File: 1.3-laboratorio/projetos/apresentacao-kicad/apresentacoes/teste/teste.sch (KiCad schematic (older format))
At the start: 19 parts

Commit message: Em elaboração, questões para a P2/2020 de ETE103/N.
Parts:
- added U?: 74AHC04, symbol 74xx:74AHC04
- added U?: 74LS04, symbol 74xx:74LS04
- added U?: IR4302, Package_DFN_QFN:Infineon_PQFN-44-31-5EP_7x7mm_P0.5mm, symbol Amplifier_Audio:IR4302
- added U?: 4002, symbol 4xxx:4002
- added U?: LM339, symbol Comparator:LM339
- added U? (x2): 74LS00, symbol 74xx:74LS00
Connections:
- new net: U?.15 (COM), U?.28 (COM), U?.31 (COM)
- new net: U?.18 (VS1), U?.20 (VS1)
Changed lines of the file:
@@
+	1    0    0    -1
+$EndComp
+$Comp
+L 74xx:74AHC04 U?
+U 1 1 5FABFB5E
+P 5250 1450
+F 0 "U?" H 5250 1767 50  0000 C CNN
+F 1 "74AHC04" H 5250 1676 50  0000 C CNN
+F 2 "" H 5250 1450 50  0001 C CNN
+F 3 "https://assets.nexperia.com/documents/data-sheet/74AHC_AHCT04.pdf" H 5250 1450 50  0001 C CNN
+	1    5250 1450
+	1    0    0    -1
+$EndComp
+$Comp
+L 74xx:74LS04 U?
+U 2 1 5FAC08BE
+P 7000 1500
+F 0 "U?" H 7000 1817 50  0000 C CNN
+F 1 "74LS04" H 7000 1726 50  0000 C CNN
+F 2 "" H 7000 1500 50  0001 C CNN
+F 3 "http://www.ti.com/lit/gpn/sn74LS04" H 7000 1500 50  0001 C CNN
+	2    7000 1500
+	1    0    0    -1
+$EndComp
+$Comp
+L Amplifier_Audio:IR4302 U?
+U 1 1 5FAC1783
+P 8400 5700
+F 0 "U?" H 8400 6681 50  0000 C CNN
+F 1 "IR4302" H 8400 6590 50  0000 C CNN
+F 2 "Package_DFN_QFN:Infineon_PQFN-44-31-5EP_7x7mm_P0.5mm" H 8400 5700 50  0001 C CIN
+F 3 "https://www.infineon.com/dgdl/ir4302.pdf?fileId=5546d462533600a4015355d602a9181d" H 8400 5700 50  0001 C CNN
+	1    8400 5700
+	1    0    0    -1
+$EndComp
+$Comp
+L 4xxx:4002 U?
+U 2 1 5FAC2A96
+P 7500 2250
+F 0 "U?" H 7500 2625 50  0000 C CNN
+F 1 "4002" H 7500 2534 50  0000 C CNN
+F 2 "" H 7500 2250 50  0001 C CNN
+F 3 "http://www.intersil.com/content/dam/Intersil/documents/cd40/cd4000bms-01bms-02bms-25bms.pdf" H 7500 2250 50  0001 C CNN
+	2    7500 2250
+	1    0    0    -1
+$EndComp
+$Comp
+L Comparator:LM339 U?
+U 2 1 5FAC41FA
+P 1550 1250
+F 0 "U?" H 1550 1617 50  0000 C CNN
+F 1 "LM339" H 1550 1526 50  0000 C CNN
+F 2 "" H 1500 1350 50  0001 C CNN
+F 3 "https://www.st.com/resource/en/datasheet/lm139.pdf" H 1600 1450 50  0001 C CNN
+	2    1550 1250
+	1    0    0    -1
+$EndComp
+$Comp
+L 74xx:74LS00 U?
+U 2 1 5FAC5635
+P 4300 1450
+F 0 "U?" H 4300 1775 50  0000 C CNN
+F 1 "74LS00" H 4300 1684 50  0000 C CNN
+F 2 "" H 4300 1450 50  0001 C CNN
+F 3 "http://www.ti.com/lit/gpn/sn74ls00" H 4300 1450 50  0001 C CNN
+	2    4300 1450
+	1    0    0    -1
+$EndComp
+$Comp
+L 74xx:74LS00 U?
+U 1 1 5FAC74AA
+P 8250 3450
+F 0 "U?" H 8250 3775 50  0000 C CNN
+F 1 "74LS00" H 8250 3684 50  0000 C CNN
+F 2 "" H 8250 3450 50  0001 C CNN
+F 3 "http://www.ti.com/lit/gpn/sn74ls00" H 8250 3450 50  0001 C CNN
+	1    8250 3450
 	1    0    0    -1
 $EndComp

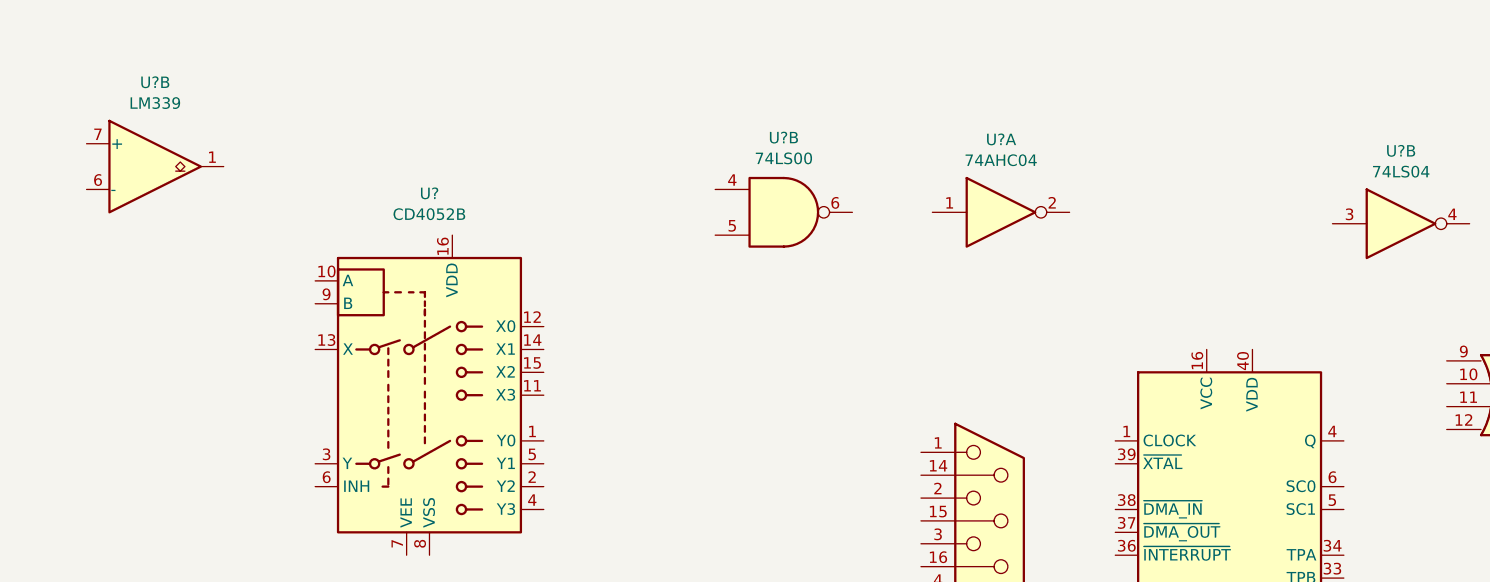
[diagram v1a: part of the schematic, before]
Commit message: Gabarito da P2/2020 de ETE103/N. Melhorias e implementações para análise de logs do Moodle, voltados para aulas de teoria. Biblioteca do Octave com função geral de carga e descarga para capacitor e indutor.
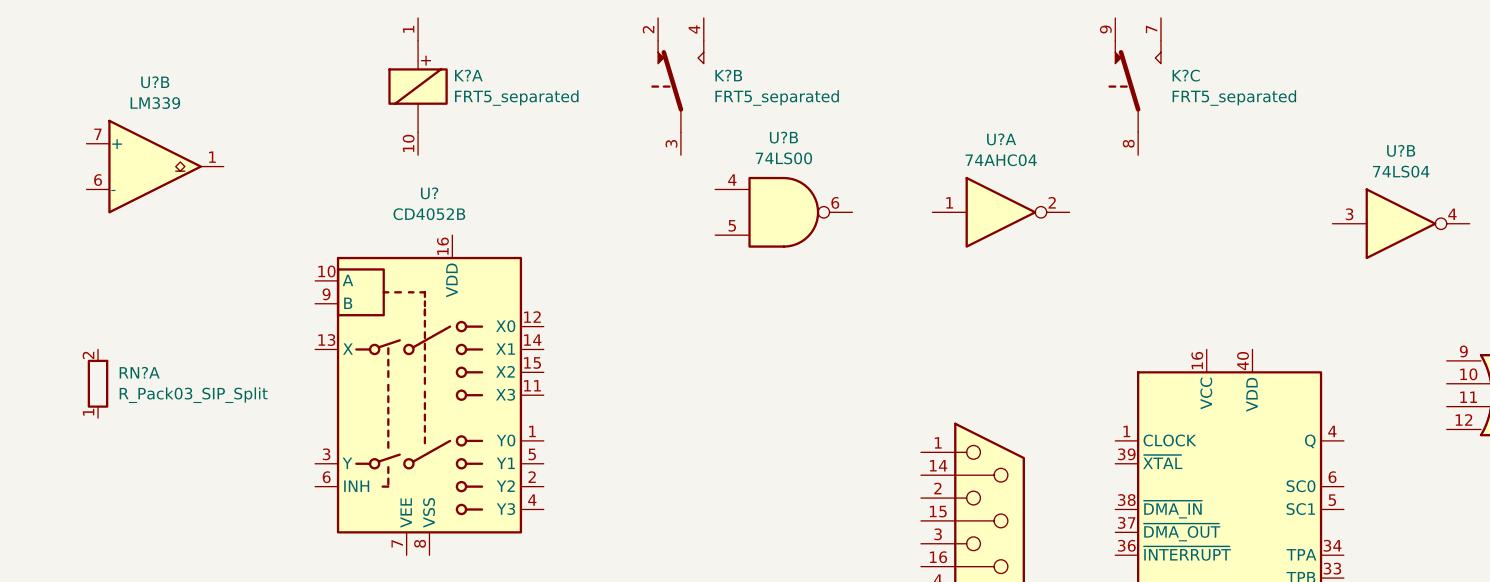
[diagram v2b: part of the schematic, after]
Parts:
- added K? (x3): FRT5_separated, Relay_THT:Relay_DPDT_FRT5, symbol Relay:FRT5_separated
- added RN?: R_Pack03_SIP_Split, Resistor_THT:R_Array_SIP6, symbol Device:R_Pack03_SIP_Split
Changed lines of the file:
@@
+	1    0    0    -1
+$EndComp
+$Comp
+L Relay:FRT5_separated K?
+U 1 1 5FBBCCFF
+P 2700 900
+F 0 "K?" H 2855 946 50  0000 L CNN
+F 1 "FRT5_separated" H 2855 855 50  0000 L CNN
+F 2 "Relay_THT:Relay_DPDT_FRT5" H 2900 800 50  0001 L CNN
+F 3 "https://www.elpro.org/de/index.php?controller=attachment&id_attachment=8663" H 2700 900 50  0001 C CNN
+	1    2700 900
+	1    0    0    -1
+$EndComp
+$Comp
+L Relay:FRT5_separated K?
+U 2 1 5FBBDEA0
+P 3850 900
+F 0 "K?" H 3994 946 50  0000 L CNN
+F 1 "FRT5_separated" H 3994 855 50  0000 L CNN
+F 2 "Relay_THT:Relay_DPDT_FRT5" H 4050 800 50  0001 L CNN
+F 3 "https://www.elpro.org/de/index.php?controller=attachment&id_attachment=8663" H 3850 900 50  0001 C CNN
+	2    3850 900
+	1    0    0    -1
+$EndComp
+$Comp
+L Relay:FRT5_separated K?
+U 3 1 5FBBEDAD
+P 5850 900
+F 0 "K?" H 5994 946 50  0000 L CNN
+F 1 "FRT5_separated" H 5994 855 50  0000 L CNN
+F 2 "Relay_THT:Relay_DPDT_FRT5" H 6050 800 50  0001 L CNN
+F 3 "https://www.elpro.org/de/index.php?controller=attachment&id_attachment=8663" H 5850 900 50  0001 C CNN
+	3    5850 900
+	1    0    0    -1
+$EndComp
+$Comp
+L Device:R_Pack03_SIP_Split RN?
+U 1 1 5FBC02C3
+P 1300 2200
+F 0 "RN?" H 1388 2246 50  0000 L CNN
+F 1 "R_Pack03_SIP_Split" H 1388 2155 50  0000 L CNN
+F 2 "Resistor_THT:R_Array_SIP6" V 1220 2200 50  0001 C CNN
+F 3 "http://www.vishay.com/docs/31509/csc.pdf" H 1300 2200 50  0001 C CNN
+	1    1300 2200
 	1    0    0    -1
 $EndComp
